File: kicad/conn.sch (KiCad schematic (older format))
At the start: 3 parts, among them J1801 Conn_02x10_Odd_Even, J1802 Conn_02x10_Odd_Even, J1803 Conn_02x10_Odd_Even

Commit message: passed all footprint, preliminarly.. and taken a pic
I've passed all 3d models, and make a pic of that, it's the first
impresion, but it need's more indeed reviews
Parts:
- removed J1801, J1802, J1803: Conn_02x10_Odd_Even, Connector_PinSocket_2.54mm:PinSocket_2x10_P2.54mm_Vertical_SMD, symbol Connector_Generic:Conn_02x10_Odd_Even
- added J1801, J1802, J1803: NHD-4.3-480272FT-CTXL-T, Connector_IDC:IDC-Header_2x10_P2.54mm_Vertical, symbol servo:NHD-4.3-480272FT-CTXL-T
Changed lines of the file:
@@
 Text Notes 6500 1200 0    197  ~ 39
 Common Connections
-$Comp
-L Connector_Generic:Conn_02x10_Odd_Even J?
-U 1 1 605AFA04
-P 9650 2850
-AR Path="/5DDE8C5E/605AFA04" Ref="J?"  Part="1"
-AR Path="/5EC40F3C/605AFA04" Ref="J1803"  Part="1"
-F 0 "J1803" H 9700 3467 50  0000 C CNN
-F 1 "Conn_02x10_Odd_Even" H 9700 3376 50  0000 C CNN
-F 2 "Connector_PinSocket_2.54mm:PinSocket_2x10_P2.54mm_Vertical_SMD" H 9650 2850 50  0001 C CNN
-F 3 "~" H 9650 2850 50  0001 C CNN
-	1    9650 2850
-	1    0    0    -1
-$EndComp
 Wire Wire Line
 	10300 2650 9950 2650
@@
 Wire Wire Line
 	9350 3350 9350 3550
-$Comp
-L Connector_Generic:Conn_02x10_Odd_Even J?
-U 1 1 605AFA33
-P 8300 4850
-AR Path="/5DDE8C5E/605AFA33" Ref="J?"  Part="1"
-AR Path="/5EC40F3C/605AFA33" Ref="J1802"  Part="1"
-F 0 "J1802" H 8350 5467 50  0000 C CNN
-F 1 "Conn_02x10_Odd_Even" H 8350 5376 50  0000 C CNN
-F 2 "Connector_PinSocket_2.54mm:PinSocket_2x10_P2.54mm_Vertical_SMD" H 8300 4850 50  0001 C CNN
-F 3 "~" H 8300 4850 50  0001 C CNN
-	1    8300 4850
-	1    0    0    -1
-$EndComp
 Wire Wire Line
 	8600 5350 8750 5350
@@
 	1    0    0    -1
 $EndComp
-$Comp
-L Connector_Generic:Conn_02x10_Odd_Even J?
-U 1 1 605C2571
-P 6750 2750
-AR Path="/5DDE8C5E/605C2571" Ref="J?"  Part="1"
-AR Path="/5EC40F3C/605C2571" Ref="J1801"  Part="1"
-F 0 "J1801" H 6800 3367 50  0000 C CNN
-F 1 "Conn_02x10_Odd_Even" H 6800 3276 50  0000 C CNN
-F 2 "Connector_PinSocket_2.54mm:PinSocket_2x10_P2.54mm_Vertical_SMD" H 6750 2750 50  0001 C CNN
-F 3 "~" H 6750 2750 50  0001 C CNN
-	1    6750 2750
-	1    0    0    -1
-$EndComp
 Wire Wire Line
 	7400 2550 7050 2550
@@
 Wire Wire Line
 	9100 3250 9450 3250
+$Comp
+L servo:NHD-4.3-480272FT-CTXL-T J?
+U 1 1 5E343D65
+P 8300 4850
+AR Path="/5E72D841/5E343D65" Ref="J?"  Part="1"
+AR Path="/5EC40F3C/5E343D65" Ref="J1802"  Part="1"
+F 0 "J1802" H 8350 5451 50  0000 C CNN
+F 1 "NHD-4.3-480272FT-CTXL-T" H 8350 5368 39  0000 C CNN
+F 2 "Connector_IDC:IDC-Header_2x10_P2.54mm_Vertical" H 8300 4850 50  0001 C CNN
+F 3 "../doc/datasheets/NHD-4.3-480272FT-CTXL-T.pdf" H 8350 5350 50  0001 C CNN
+	1    8300 4850
+	1    0    0    -1
+$EndComp
+$Comp
+L servo:NHD-4.3-480272FT-CTXL-T J?
+U 1 1 5E34A399
+P 6750 2750
+AR Path="/5E72D841/5E34A399" Ref="J?"  Part="1"
+AR Path="/5EC40F3C/5E34A399" Ref="J1801"  Part="1"
+F 0 "J1801" H 6800 3351 50  0000 C CNN
+F 1 "NHD-4.3-480272FT-CTXL-T" H 6800 3268 39  0000 C CNN
+F 2 "Connector_IDC:IDC-Header_2x10_P2.54mm_Vertical" H 6750 2750 50  0001 C CNN
+F 3 "../doc/datasheets/NHD-4.3-480272FT-CTXL-T.pdf" H 6800 3250 50  0001 C CNN
+	1    6750 2750
+	1    0    0    -1
+$EndComp
+$Comp
+L servo:NHD-4.3-480272FT-CTXL-T J?
+U 1 1 5E350A93
+P 9650 2850
+AR Path="/5E72D841/5E350A93" Ref="J?"  Part="1"
+AR Path="/5EC40F3C/5E350A93" Ref="J1803"  Part="1"
+F 0 "J1803" H 9700 3451 50  0000 C CNN
+F 1 "NHD-4.3-480272FT-CTXL-T" H 9700 3368 39  0000 C CNN
+F 2 "Connector_IDC:IDC-Header_2x10_P2.54mm_Vertical" H 9650 2850 50  0001 C CNN
+F 3 "../doc/datasheets/NHD-4.3-480272FT-CTXL-T.pdf" H 9700 3350 50  0001 C CNN
+	1    9650 2850
+	1    0    0    -1
+$EndComp
 $EndSCHEMATC

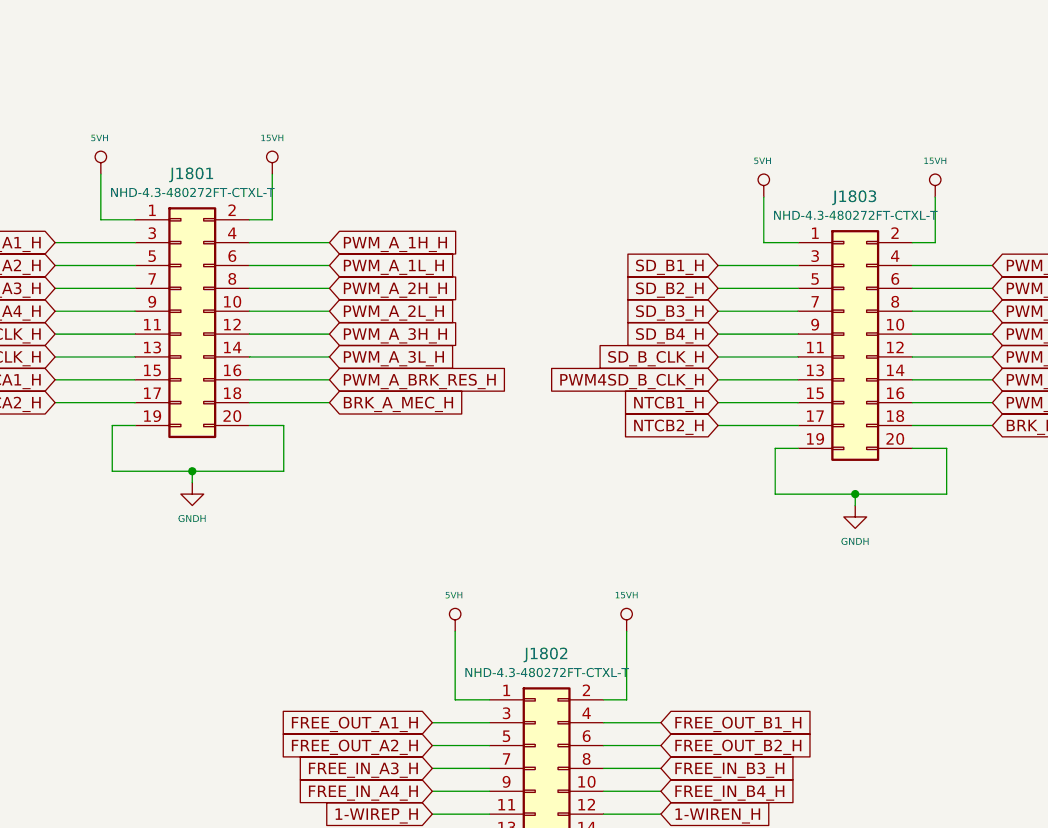
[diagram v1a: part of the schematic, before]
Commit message: changing single row terminal block to double row
I've changed to double row all the connectors, RJ45 and terminal blocks,
I saves spaces and also make it more intuitive related to user
interface..lets go
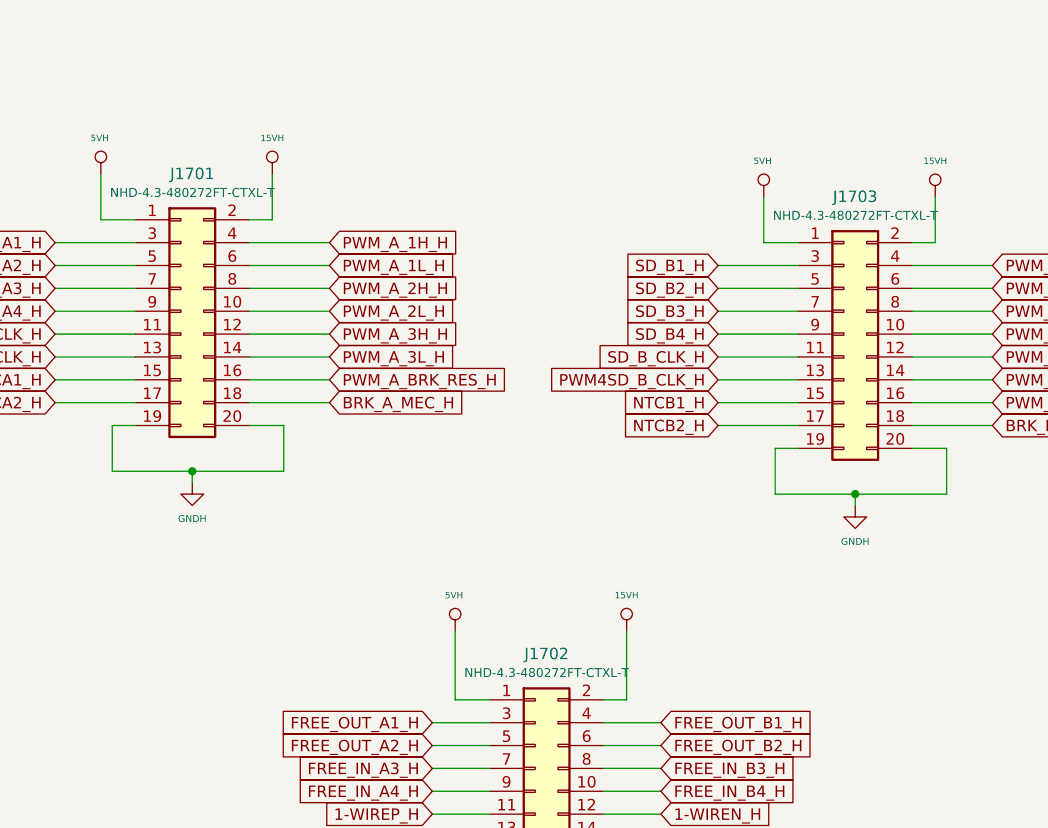
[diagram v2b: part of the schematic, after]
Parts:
- renumbered J1801 to J1701, J1802 to J1702, J1803 to J1703
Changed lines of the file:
@@
 $Descr A3 16535 11693
 encoding utf-8
-Sheet 18 19
+Sheet 18 18
 Title "Common connections"
 Date "2020-01-09"
@@
 P 9700 3600
 AR Path="/5DDE8C5E/605AFA1C" Ref="#PWR?"  Part="1"
-AR Path="/5EC40F3C/605AFA1C" Ref="#PWR01808"  Part="1"
-F 0 "#PWR01808" H 9700 3350 30  0001 C CNN
+AR Path="/5EC40F3C/605AFA1C" Ref="#PWR01708"  Part="1"
+F 0 "#PWR01708" H 9700 3350 30  0001 C CNN
 F 1 "GNDH" H 9700 3442 30  0000 C CNN
 F 2 "" H 9700 3600 50  0001 C CNN
@@
 P 9300 2250
 AR Path="/5DDE8C5E/605AFA23" Ref="#PWR?"  Part="1"
-AR Path="/5EC40F3C/605AFA23" Ref="#PWR01807"  Part="1"
-F 0 "#PWR01807" H 9300 2050 20  0001 C CNN
+AR Path="/5EC40F3C/605AFA23" Ref="#PWR01707"  Part="1"
+F 0 "#PWR01707" H 9300 2050 20  0001 C CNN
 F 1 "5VH" H 9305 2407 28  0000 C CNN
 F 2 "" H 9300 2250 50  0001 C CNN
@@
 P 8350 5600
 AR Path="/5DDE8C5E/605AFA3B" Ref="#PWR?"  Part="1"
-AR Path="/5EC40F3C/605AFA3B" Ref="#PWR01805"  Part="1"
-F 0 "#PWR01805" H 8350 5350 30  0001 C CNN
+AR Path="/5EC40F3C/605AFA3B" Ref="#PWR01705"  Part="1"
+F 0 "#PWR01705" H 8350 5350 30  0001 C CNN
 F 1 "GNDH" H 8350 5442 30  0000 C CNN
 F 2 "" H 8350 5600 50  0001 C CNN
@@
 P 7950 4150
 AR Path="/5DDE8C5E/605AFA42" Ref="#PWR?"  Part="1"
-AR Path="/5EC40F3C/605AFA42" Ref="#PWR01804"  Part="1"
-F 0 "#PWR01804" H 7950 3950 20  0001 C CNN
+AR Path="/5EC40F3C/605AFA42" Ref="#PWR01704"  Part="1"
+F 0 "#PWR01704" H 7950 3950 20  0001 C CNN
 F 1 "5VH" H 7955 4307 28  0000 C CNN
 F 2 "" H 7950 4150 50  0001 C CNN
@@
 P 10050 2250
 AR Path="/5DDE8C5E/605AFA8F" Ref="#PWR?"  Part="1"
-AR Path="/5EC40F3C/605AFA8F" Ref="#PWR01809"  Part="1"
-F 0 "#PWR01809" H 10050 2050 20  0001 C CNN
+AR Path="/5EC40F3C/605AFA8F" Ref="#PWR01709"  Part="1"
+F 0 "#PWR01709" H 10050 2050 20  0001 C CNN
 F 1 "15VH" H 10050 2407 28  0000 C CNN
 F 2 "" H 10050 2250 50  0001 C CNN
@@
 P 6800 3500
 AR Path="/5DDE8C5E/605C2589" Ref="#PWR?"  Part="1"
-AR Path="/5EC40F3C/605C2589" Ref="#PWR01802"  Part="1"
-F 0 "#PWR01802" H 6800 3250 30  0001 C CNN
+AR Path="/5EC40F3C/605C2589" Ref="#PWR01702"  Part="1"
+F 0 "#PWR01702" H 6800 3250 30  0001 C CNN
 F 1 "GNDH" H 6800 3342 30  0000 C CNN
 F 2 "" H 6800 3500 50  0001 C CNN
@@
 P 6400 2150
 AR Path="/5DDE8C5E/605C2590" Ref="#PWR?"  Part="1"
-AR Path="/5EC40F3C/605C2590" Ref="#PWR01801"  Part="1"
-F 0 "#PWR01801" H 6400 1950 20  0001 C CNN
+AR Path="/5EC40F3C/605C2590" Ref="#PWR01701"  Part="1"
+F 0 "#PWR01701" H 6400 1950 20  0001 C CNN
 F 1 "5VH" H 6405 2307 28  0000 C CNN
 F 2 "" H 6400 2150 50  0001 C CNN
@@
 P 7150 2150
 AR Path="/5DDE8C5E/605C25AF" Ref="#PWR?"  Part="1"
-AR Path="/5EC40F3C/605C25AF" Ref="#PWR01803"  Part="1"
-F 0 "#PWR01803" H 7150 1950 20  0001 C CNN
+AR Path="/5EC40F3C/605C25AF" Ref="#PWR01703"  Part="1"
+F 0 "#PWR01703" H 7150 1950 20  0001 C CNN
 F 1 "15VH" H 7150 2307 28  0000 C CNN
 F 2 "" H 7150 2150 50  0001 C CNN
@@
 P 8700 4150
 AR Path="/5DDE8C5E/60686BCE" Ref="#PWR?"  Part="1"
-AR Path="/5EC40F3C/60686BCE" Ref="#PWR01806"  Part="1"
-F 0 "#PWR01806" H 8700 3950 20  0001 C CNN
+AR Path="/5EC40F3C/60686BCE" Ref="#PWR01706"  Part="1"
+F 0 "#PWR01706" H 8700 3950 20  0001 C CNN
 F 1 "15VH" H 8700 4307 28  0000 C CNN
 F 2 "" H 8700 4150 50  0001 C CNN
@@
 P 8300 4850
 AR Path="/5E72D841/5E343D65" Ref="J?"  Part="1"
-AR Path="/5EC40F3C/5E343D65" Ref="J1802"  Part="1"
-F 0 "J1802" H 8350 5451 50  0000 C CNN
+AR Path="/5EC40F3C/5E343D65" Ref="J1702"  Part="1"
+F 0 "J1702" H 8350 5451 50  0000 C CNN
 F 1 "NHD-4.3-480272FT-CTXL-T" H 8350 5368 39  0000 C CNN
 F 2 "Connector_IDC:IDC-Header_2x10_P2.54mm_Vertical" H 8300 4850 50  0001 C CNN
@@
 P 6750 2750
 AR Path="/5E72D841/5E34A399" Ref="J?"  Part="1"
-AR Path="/5EC40F3C/5E34A399" Ref="J1801"  Part="1"
-F 0 "J1801" H 6800 3351 50  0000 C CNN
+AR Path="/5EC40F3C/5E34A399" Ref="J1701"  Part="1"
+F 0 "J1701" H 6800 3351 50  0000 C CNN
 F 1 "NHD-4.3-480272FT-CTXL-T" H 6800 3268 39  0000 C CNN
 F 2 "Connector_IDC:IDC-Header_2x10_P2.54mm_Vertical" H 6750 2750 50  0001 C CNN
@@
 P 9650 2850
 AR Path="/5E72D841/5E350A93" Ref="J?"  Part="1"
-AR Path="/5EC40F3C/5E350A93" Ref="J1803"  Part="1"
-F 0 "J1803" H 9700 3451 50  0000 C CNN
+AR Path="/5EC40F3C/5E350A93" Ref="J1703"  Part="1"
+F 0 "J1703" H 9700 3451 50  0000 C CNN
 F 1 "NHD-4.3-480272FT-CTXL-T" H 9700 3368 39  0000 C CNN
 F 2 "Connector_IDC:IDC-Header_2x10_P2.54mm_Vertical" H 9650 2850 50  0001 C CNN
